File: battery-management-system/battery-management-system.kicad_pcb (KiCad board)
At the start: 4 copper layers, 130 x 100 mm, 216 parts, among them J1 CELL4_PLUS, J10 9V4, J11 5V, J12 18V, J13 3V3, J14 AMPHENOL_micro_usb_10118194-0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, J16 I2C, J17 UART_INTERCONNECT, J18 LEDS, J19 CHARGE/DISCHARGE, J2 CELL4_MINUS, J20 UART_USB, J21 rspro_header_5pin_3_5mm, J22 TEMP_CELL1, J23 TEMP_CELL2, J24 TEMP_CELL3, J25 TEMP_CELL4, J26 BALANCE_CONTROL, J27 BALANCE_INPUTS, J28 BALANCE_CURRENT, J3 CELL3_MINUS, J4 CELL2_MINUS, J5 CELL1_MINUS, J6 VBAT+, J7 VBAT+_CHARGE, J8 VBAT-, J9 -5V, Q1 DMN3730U, Q10 BS250FTA, Q11 BS250FTA, Q12 BS250FTA, Q13 BS250FTA, Q14 DMN3730U, Q15 DMN3404L, Q16 DMN3730U, Q17 DMN3730U, Q18 DMN3730U, Q19 DMN3730U, Q2 TJ40S04M3L, Q3 TJ40S04M3L, Q4 DMN3730U, Q5 DMN3730U, Q6 DMN3730U, Q7 DMN3730U, Q8 DMN3730U, Q9 DMN3730U, SW1 CELL4_PLUS, SW2 CELL4_MINUS, SW3 CELL3_PLUS, SW4 CELL3_MINUS, SW5 CELL2_PLUS, SW6 CELL2_MINUS, SW7 CELL1_PLUS, SW8 CELL1_MINUS, U1 ICL7660, U10 STC3100, U11 STM32L071CZTx, U12 LM2904M8-13, U13 LM2904M8-13, U14 LM2904M8-13, U15 LM2904M8-13, U16 MC74VHC139, U2 ICL7660, U3 L6982C33DR, U4 L6982C33DR, U5 ICL7660, U6 FT230XS, U7 ARM-JTAG-SWD, U8 AT24C512C, U9 NCT75DR2G

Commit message: update footprints and layout
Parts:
- removed C48: 90F, benediktibk:vishay_super_cap_form_g
- moved C46 10.2 mm to (67.1, 84.0)
- moved C47 0.50 mm to (67.1, 89.4), turned to 180 degrees
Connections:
- C46 pad 1: /BALANCE_CAP_MINUS_RAW -> /BALANCE_CAP_PLUS_RAW
- C46 pad 2: /BALANCE_CAP_PLUS_RAW -> /BALANCE_CAP_MINUS_RAW
- C47 pad 1: /BALANCE_CAP_MINUS_RAW -> /BALANCE_CAP_PLUS_RAW
- C47 pad 2: /BALANCE_CAP_PLUS_RAW -> /BALANCE_CAP_MINUS_RAW
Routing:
- net /BALANCE_CAP_MINUS_RAW: track 103.9 -> 86.5 mm, vias 0 -> 1
- net /BALANCE_CAP_PLUS_RAW: track 120.4 -> 105.5 mm

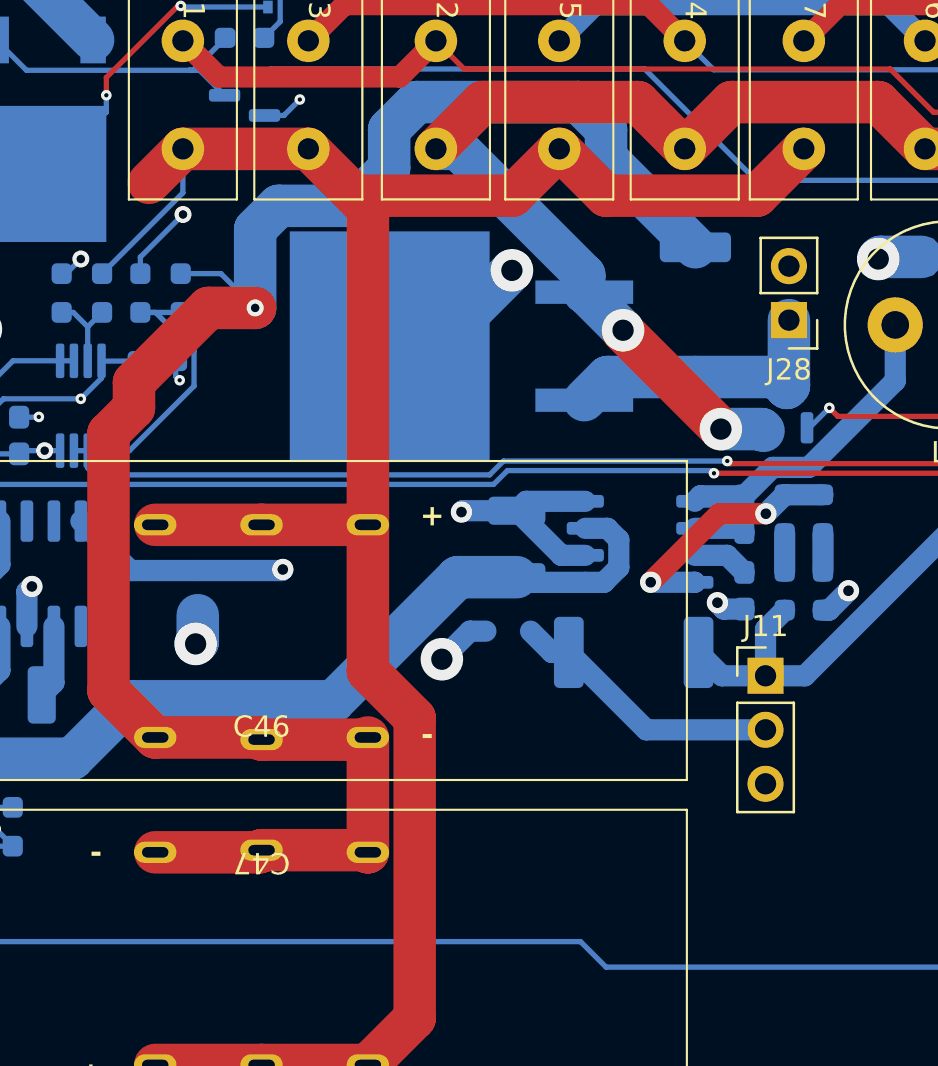
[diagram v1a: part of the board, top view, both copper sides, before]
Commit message: fix design rule errors
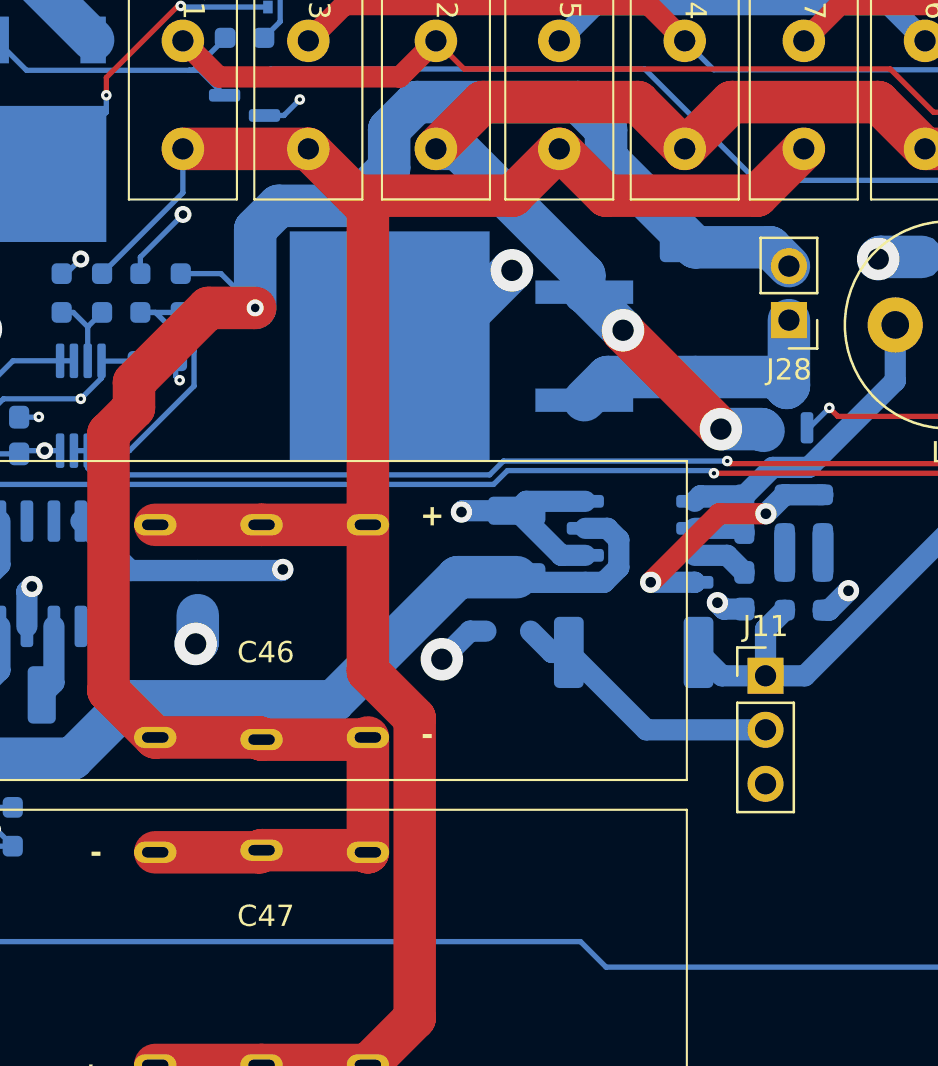
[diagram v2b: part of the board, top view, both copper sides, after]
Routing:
- net Net-(D10-K): track 111.9 -> 100.8 mm
- net /BALANCE_CAP_MINUS_RAW: track 86.5 -> 91.3 mm
- net /5V: track 262.1 -> 265.2 mm
- net /BALANCE_CAP_PLUS_RAW: track 105.5 -> 103.2 mm
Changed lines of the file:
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@@
     (property "ki_keywords" "cap capacitor")
     (attr through_hole)
-    (fp_text reference "C46" (at 0 -0.5 unlocked) (layer "F.SilkS")
+    (fp_text reference "C46" (at 0.2 -4 unlocked) (layer "F.SilkS")
         (effects (font (size 1 1) (thickness 0.15)))
     )
@@
     (property "ki_keywords" "cap capacitor")
     (attr through_hole)
-    (fp_text reference "C47" (at 0 -0.5 180 unlocked) (layer "F.SilkS")
+    (fp_text reference "C47" (at -0.2 -3 unlocked) (layer "F.SilkS")
         (effects (font (size 1 1) (thickness 0.15)))
     )
@@
   (via (at 39.3 93.3) (size 1) (drill 0.5) (layers "F.Cu" "B.Cu") (net 11))
   (via (at 86.3 115.8005) (size 2) (drill 1) (layers "F.Cu" "B.Cu") (net 11))
-  (segment (start 80.869848 92) (end 70.88873 92) (width 2) (layer "In1.Cu") (net 11))
-  (segment (start 39.83355 92.165001) (end 38.999275 92.999276) (width 2) (layer "In1.Cu") (net 11))
-  (segment (start 80.869848 92) (end 86.3 97.430152) (width 2) (layer "In1.Cu") (net 11))
-  (segment (start 45.6 93.160837) (end 44.604164 92.165001) (width 2) (layer "In1.Cu") (net 11))
-  (segment (start 47.008328 93.160837) (end 45.6 93.160837) (width 2) (layer "In1.Cu") (net 11))
-  (segment (start 70.88873 92) (end 62.044365 83.155635) (width 2) (layer "In1.Cu") (net 11))
-  (segment (start 44.604164 92.165001) (end 39.83355 92.165001) (width 2) (layer "In1.Cu") (net 11))
-  (segment (start 62.044365 81.855635) (end 56.662036 81.855635) (width 2) (layer "In1.Cu") (net 11))
-  (segment (start 86.3 97.430152) (end 86.3 115.8005) (width 2) (layer "In1.Cu") (net 11))
-  (segment (start 56.662036 81.855635) (end 56.662036 83.507129) (width 2) (layer "In1.Cu") (net 11))
-  (segment (start 62.044365 83.155635) (end 62.044365 81.855635) (width 2) (layer "In1.Cu") (net 11))
-  (segment (start 56.662036 83.507129) (end 47.008328 93.160837) (width 2) (layer "In1.Cu") (net 11))
+  (segment (start 86.3 115.8005) (end 86.3 97.430152) (width 2) (layer "In1.Cu") (net 11))
+  (segment (start 81.219848 92.35) (end 44.789163 92.35) (width 2) (layer "In1.Cu") (net 11))
+  (segment (start 44.604164 92.165001) (end 43.195836 92.165001) (width 2) (layer "In1.Cu") (net 11))
+  (segment (start 86.3 97.430152) (end 81.219848 92.35) (width 2) (layer "In1.Cu") (net 11))
+  (segment (start 39.648551 92.35) (end 38.999275 92.999276) (width 2) (layer "In1.Cu") (net 11))
+  (segment (start 43.010837 92.35) (end 39.648551 92.35) (width 2) (layer "In1.Cu") (net 11))
+  (segment (start 44.789163 92.35) (end 44.604164 92.165001) (width 2) (layer "In1.Cu") (net 11))
+  (segment (start 43.195836 92.165001) (end 43.010837 92.35) (width 2) (layer "In1.Cu") (net 11))
   (segment (start 88.0995 117.6) (end 86.3 115.8005) (width 1) (layer "B.Cu") (net 11))
   (segment (start 39.1 93.5) (end 39.3 93.3) (width 1) (layer "B.Cu") (net 11))
@@
   (segment (start 83.3 55.40873) (end 82.01127 54.12) (width 2) (layer "B.Cu") (net 12))
   (segment (start 73.1 55.40873) (end 73.1 57.23127) (width 2) (layer "B.Cu") (net 12))
+  (segment (start 91.015 60.95) (end 91.9 61.835) (width 2) (layer "B.Cu") (net 12))
+  (segment (start 87.5 60.95) (end 91.015 60.95) (width 2) (layer "B.Cu") (net 12))
   (segment (start 87.5 60.95) (end 83.3 56.75) (width 2) (layer "B.Cu") (net 12))
   (segment (start 67.9 59) (end 66.8 60.1) (width 2) (layer "B.Cu") (net 12))
@@
   (segment (start 67.1 99.4) (end 72.1 99.4) (width 2) (layer "F.Cu") (net 14))
   (segment (start 69.3 56.32) (end 71.5 58.52) (width 2) (layer "F.Cu") (net 14))
-  (segment (start 61.8 57.92) (end 63.4 56.32) (width 2) (layer "F.Cu") (net 14))
   (segment (start 72.1 80.88873) (end 74.3 83.08873) (width 2) (layer "F.Cu") (net 14))
   (segment (start 69.3 56.32) (end 63.4 56.32) (width 2) (layer "F.Cu") (net 14))
@@
   (via (at 125.9 38.8) (size 0.5) (drill 0.2) (layers "F.Cu" "B.Cu") (net 39))
   (via (at 68.1 76.1) (size 1) (drill 0.5) (layers "F.Cu" "B.Cu") (net 39))
+  (segment (start 61.516663 70.5125) (end 64.5 73.495837) (width 2) (layer "In1.Cu") (net 39))
   (segment (start 65.6 48.36) (end 65.6 61.8) (width 2) (layer "In1.Cu") (net 39))
-  (segment (start 75.578769 80.321231) (end 71.257538 76) (width 2) (layer "In1.Cu") (net 39))
   (segment (start 106.261 48.1) (end 117.05061 48.1) (width 2) (layer "In1.Cu") (net 39))
   (segment (start 118.99061 46.16) (end 121.95 49.11939) (width 2) (layer "In1.Cu") (net 39))
@@
   (segment (start 63.4 46.16) (end 65.6 48.36) (width 2) (layer "In1.Cu") (net 39))
   (segment (start 92.6 46.16) (end 87 46.16) (width 2) (layer "In1.Cu") (net 39))
+  (segment (start 66.295837 76.1) (end 71.357538 76.1) (width 2) (layer "In1.Cu") (net 39))
   (segment (start 121.95 49.11939) (end 121.95 59.6995) (width 2) (layer "In1.Cu") (net 39))
   (segment (start 65.6 61.8) (end 61 66.4) (width 2) (layer "In1.Cu") (net 39))
+  (segment (start 64.5 74.304163) (end 66.295837 76.1) (width 2) (layer "In1.Cu") (net 39))
   (segment (start 117.05061 48.1) (end 118.99061 46.16) (width 2) (layer "In1.Cu") (net 39))
   (segment (start 61 66.4) (end 61 69.01127) (width 2) (layer "In1.Cu") (net 39))
-  (segment (start 67.98873 76) (end 61 69.01127) (width 2) (layer "In1.Cu") (net 39))
+  (segment (start 66.295837 76.1) (end 68.1 76.1) (width 2) (layer "In1.Cu") (net 39))
   (segment (start 81.121231 80.321231) (end 75.578769 80.321231) (width 2) (layer "In1.Cu") (net 39))
   (segment (start 69.3 46.16) (end 75.3 46.16) (width 2) (layer "In1.Cu") (net 39))
   (segment (start 106.91 61.01) (end 106.625 60.725) (width 2) (layer "In1.Cu") (net 39))
+  (segment (start 64.5 73.495837) (end 64.5 74.304163) (width 2) (layer "In1.Cu") (net 39))
   (segment (start 98.3 46.16) (end 92.6 46.16) (width 2) (layer "In1.Cu") (net 39))
+  (segment (start 59.49877 70.5125) (end 61.516663 70.5125) (width 2) (layer "In1.Cu") (net 39))
   (segment (start 118.99061 46.16) (end 123.95 41.20061) (width 2) (layer "In1.Cu") (net 39))
   (segment (start 92.6 44.7) (end 90.9 43) (width 2) (layer "In1.Cu") (net 39))
-  (segment (start 71.257538 76) (end 67.98873 76) (width 2) (layer "In1.Cu") (net 39))
   (segment (start 59.49877 70.5125) (end 56.9 70.5125) (width 2) (layer "In1.Cu") (net 39))
   (segment (start 81.1 46.16) (end 75.3 46.16) (width 2) (layer "In1.Cu") (net 39))
@@
   (segment (start 81.1 46.16) (end 87 46.16) (width 2) (layer "In1.Cu") (net 39))
   (segment (start 125.14939 38.8) (end 125.9 38.8) (width 2) (layer "In1.Cu") (net 39))
+  (segment (start 71.357538 76.1) (end 75.578769 80.321231) (width 2) (layer "In1.Cu") (net 39))
   (segment (start 109.5 115) (end 109.5 108.7) (width 2) (layer "In1.Cu") (net 39))
   (segment (start 106.0005 48.3605) (end 106.261 48.1) (width 2) (layer "In1.Cu") (net 39))

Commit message: add enable input for cell measurement
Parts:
- removed the C2 at (55.2, 82.0)
- removed the C34 at (77.6, 42.7)
- removed C37, C39, C40, C42, C43: 100nF, benediktibk:C_0603_1608Metric_Pad1.08x0.95mm_HandSolder
- removed C41, C44: 1uF, benediktibk:C_0603_1608Metric_Pad1.08x0.95mm_HandSolder
- removed C46, C47: 90F, benediktibk:vishay_super_cap_form_g
- removed the C5 at (50.8, 78.3)
- removed D22, D23, D24, D25: BAS416, benediktibk:D_SOD-323
- removed the J10 at (126.9, 50.5)
- removed J26: BALANCE_CONTROL, benediktibk:PinHeader_1x05_P2.54mm_Vertical
- removed J27: BALANCE_INPUTS, benediktibk:PinHeader_1x05_P2.54mm_Vertical
- removed J28: BALANCE_CURRENT, benediktibk:PinHeader_1x02_P2.54mm_Vertical
- removed the J9 at (44.4, 82.9)
- removed the R47 at (59.6, 63.1)
- removed the R48 at (57.7, 63.1)
- removed the R49 at (63.3, 63.1)
- removed the R50 at (61.4, 63.1)
- removed R59: 100kOhm, benediktibk:R_0603_1608Metric_Pad0.98x0.95mm_HandSolder
- removed the R6 at (47.0, 76.9)
- removed R60, R61: 10kOhm, benediktibk:R_0603_1608Metric_Pad0.98x0.95mm_HandSolder
- removed R62: 220kOhm, benediktibk:R_0603_1608Metric_Pad0.98x0.95mm_HandSolder
- removed R63: 4Ohm, benediktibk:TO-263-resistor
- removed R64: 2mOhm, benediktibk:R_2512_6332Metric_Pad1.40x3.35mm_HandSolder
- removed the R7 at (123.0, 53.2)
- removed SW1: CELL4_PLUS, benediktibk:SIL05-1A72-BV669
- removed SW2: CELL4_MINUS, benediktibk:SIL05-1A72-BV669
- removed SW3: CELL3_PLUS, benediktibk:SIL05-1A72-BV669
- removed SW4: CELL3_MINUS, benediktibk:SIL05-1A72-BV669
- removed SW5: CELL2_PLUS, benediktibk:SIL05-1A72-BV669
- removed SW6: CELL2_MINUS, benediktibk:SIL05-1A72-BV669
- removed SW7: CELL1_PLUS, benediktibk:SIL05-1A72-BV669
- removed SW8: CELL1_MINUS, benediktibk:SIL05-1A72-BV669
- removed the U13 at (58.6, 68.4)
- removed U15: LM2904M8-13, benediktibk:MSOP-8_3x3mm_P0.65mm
- removed the U2 at (56.7, 76.3)
- added H4: MountingHole_Pad, benediktibk:MountingHole_6.4mm_M6_Pad_TopBottom, F.Cu at (28.0, 152.0)
- added J23: Conn_01x05, benediktibk:PinHeader_1x05_P2.54mm_Vertical, F.Cu at (48.8, 131.8)
- added L10: L_220µH_1A, benediktibk:L_Wuerth_HCI-1050, B.Cu at (66.0, 83.0)
- added L3: L_220µH_1A, benediktibk:L_Wuerth_HCI-1050, B.Cu at (92.0, 44.0)
- added L4: L_220µH_1A, benediktibk:L_Wuerth_HCI-1050, B.Cu at (92.0, 57.0)
- added L5: L_220µH_1A, benediktibk:L_Wuerth_HCI-1050, B.Cu at (92.0, 70.0)
- added L6: L_220µH_1A, benediktibk:L_Wuerth_HCI-1050, B.Cu at (92.0, 83.0)
- added L7: L_220µH_1A, benediktibk:L_Wuerth_HCI-1050, B.Cu at (79.0, 83.0)
- added L8: L_220µH_1A, benediktibk:L_Wuerth_HCI-1050, B.Cu at (79.0, 70.0)
- added L9: L_220µH_1A, benediktibk:L_Wuerth_HCI-1050, B.Cu at (66.0, 70.0)
- added Q20: DMN3404L, benediktibk:SOT-23, B.Cu at (40.0, 66.0)
- added Q21: DMN3404L, benediktibk:SOT-23, B.Cu at (101.0, 73.0)
- added Q22: DMN3404L, benediktibk:SOT-23, B.Cu at (101.0, 43.0)
- added Q23: DMN3404L, benediktibk:SOT-23, B.Cu at (40.0, 50.0)
- added Q24: DMN3404L, benediktibk:SOT-23, B.Cu at (45.0, 55.0)
- added Q25: DMN3404L, benediktibk:SOT-23, B.Cu at (101.0, 58.0)
- added Q26: DMN3404L, benediktibk:SOT-23, B.Cu at (101.0, 68.0)
- added Q27: DMN3404L, benediktibk:SOT-23, B.Cu at (45.0, 61.0)
- added Q28: DMN3404L, benediktibk:SOT-23, B.Cu at (45.0, 66.0)
- added Q29: DMN3404L, benediktibk:SOT-23, B.Cu at (101.0, 78.0)
- added Q30: DMN3404L, benediktibk:SOT-23, B.Cu at (101.0, 83.0)
- added Q31: DMN3404L, benediktibk:SOT-23, B.Cu at (101.0, 48.0)
- added Q32: DMN3404L, benediktibk:SOT-23, B.Cu at (101.0, 87.8)
- added Q33: DMN3404L, benediktibk:SOT-23, B.Cu at (51.0, 66.1)
- added Q34: DMN3404L, benediktibk:SOT-23, B.Cu at (49.9, 56.0)
- added Q35: DMN3404L, benediktibk:SOT-23, B.Cu at (83.4, 43.8)
- added Q36: DMN3404L, benediktibk:SOT-23, B.Cu at (96.7, 91.1)
- added Q37: DMN3404L, benediktibk:SOT-23, B.Cu at (111.3, 94.2)
- added Q38: TJ40S04M3L, benediktibk:TO-252-2, B.Cu at (103.9, 95.9)
- added R52: 10kOhm, benediktibk:R_0603_1608Metric_Pad0.98x0.95mm_HandSolder, B.Cu at (104.0, 87.8)
- added R53: 10kOhm, benediktibk:R_0603_1608Metric_Pad0.98x0.95mm_HandSolder, B.Cu at (51.1, 63.2)
- added R54: 10kOhm, benediktibk:R_0603_1608Metric_Pad0.98x0.95mm_HandSolder, B.Cu at (49.8, 58.8)
- added R55: 10kOhm, benediktibk:R_0603_1608Metric_Pad0.98x0.95mm_HandSolder, B.Cu at (83.2, 46.8)
- added R56: 10kOhm, benediktibk:R_0603_1608Metric_Pad0.98x0.95mm_HandSolder, B.Cu at (93.7, 91.1)
- added R57: 220kOhm, benediktibk:R_0603_1608Metric_Pad0.98x0.95mm_HandSolder, B.Cu at (108.6, 93.4)
- Q1, Q14, Q16, Q17, Q18, Q19, Q4, Q5, Q6, Q7, Q8, Q9: value DMN3730U -> DMN3404L
- moved C22 138.4 mm to (259.3, 124.9)
- moved C23 138.4 mm to (210.8, 142.3)
- moved C24 138.4 mm to (248.3, 141.4)
- moved C27 138.4 mm to (259.6, 129.8)
- moved C28 138.4 mm to (259.6, 134.9)
- moved C32 138.4 mm to (209.8, 85.3)
- moved D19 138.4 mm to (276.3, 88.5)
- moved D20 138.4 mm to (276.3, 85.8)
- moved D21 138.4 mm to (276.3, 83.3)
- moved J12 138.4 mm to (153.8, 140.9)
- moved J13 138.4 mm to (228.2, 148.9)
- moved J15 138.4 mm to (279.8, 88.4)
- moved Q6 138.4 mm to (276.3, 89.2)
- moved Q7 138.4 mm to (276.3, 85.0)
- moved Q8 138.4 mm to (276.3, 80.8)
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- renumbered C12 to C10, C13 to C11, C14 to C12, C15 to C13, C16 to C14, C17 to C15, C18 to C16, C19 to C17, C20 to C18, C21 to C19, C3 to C2, C22 to C20, C23 to C21, C24 to C22, C25 to C23, C26 to C24, C27 to C25, C28 to C26, C29 to C27, C30 to C28, C31 to C29, C4 to C3, C32 to C30, C33 to C31, C35 to C32, C36 to C33, C38 to C34, C45 to C35, C6 to C4, C7 to C5, C8 to C6, C9 to C7, C10 to C8, C11 to C9, J12 to J10, J13 to J11, J14 to J12, J16 to J13, J17 to J14, J18 to J15, J19 to J16, J20 to J17, J21 to J18, J22 to J19, J23 to J20, J24 to J21, J25 to J22, J11 to J9, R12 to R10, R13 to R11, R14 to R12, R15 to R13, R16 to R14, R17 to R15, R18 to R16, R19 to R17, R20 to R18, R21 to R19, R22 to R20, R23 to R21, R24 to R22, R25 to R23, R26 to R24, R27 to R25, R29 to R26, R30 to R27, R31 to R28, R32 to R29, R33 to R30, R34 to R31, R35 to R32, R36 to R33, R37 to R34, R38 to R35, R39 to R36, R40 to R37, R41 to R38, R42 to R39, R43 to R40, R44 to R41, R45 to R42, R46 to R43, R51 to R44, R52 to R45, R53 to R46, R54 to R47, R55 to R48, R56 to R49, R57 to R50, R58 to R51, R8 to R6, R9 to R7, R10 to R8, R11 to R9, U11 to U10, U12 to U11, U14 to U12, U16 to U13, U3 to U2, U4 to U3, U5 to U4, U6 to U5, U7 to U6, U8 to U7, U9 to U8, U10 to U9
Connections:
- C32 pad 2: /-5V -> GND
- C34 pad 2: /-5V -> GND
- D12 pad 2: Net-(D12-A) -> /Power Supply/9V4
- Q14 pad 1: /LIMIT_BALANCING_CURRENT -> /Cell Balancing/CHARGE_CELL4
- Q14 pad 2: GND -> /Battery Pack/PACK
- Q15 pad 1: Net-(Q14-D) -> /Cell Balancing/CHARGE_CELL4
- Q15 pad 3: Net-(J28-Pin_1) -> /Battery Pack/CELL4_MINUS
- Q16 pad 1: Net-(Q16-G) -> /Cell Balancing/CHARGE_CELL3
- Q16 pad 2: GND -> /Battery Pack/CELL4_MINUS
- Q16 pad 3: /Cell Balancing/CELL1 -> Net-(Q16-D)
- Q17 pad 1: Net-(Q17-G) -> /Cell Balancing/CHARGE_CELL3
- Q17 pad 2: GND -> Net-(Q17-S)
- Q17 pad 3: /Cell Balancing/CELL2 -> /Battery Pack/CELL3_MINUS
- Q18 pad 1: Net-(Q18-G) -> /Cell Balancing/CHARGE_CELL2
- Q18 pad 2: GND -> /Battery Pack/CELL3_MINUS
- Q18 pad 3: /Cell Balancing/CELL3 -> Net-(Q18-D)
- Q19 pad 1: Net-(Q19-G) -> /Cell Balancing/CHARGE_CELL2
- Q19 pad 2: GND -> Net-(Q19-S)
- Q19 pad 3: /Cell Balancing/CELL4 -> /Battery Pack/CELL2_MINUS
- U10 pad 14: /Cell Measurement/BALANCE_CAP_PLUS -> unconnected-(U10-PA4-Pad14)
- U10 pad 15: /Cell Measurement/BALANCE_CAP_MINUS -> unconnected-(U10-PA5-Pad15)
- U10 pad 38: /DISCHARGE -> /CELL_BALANCING_STROBE
- U10 pad 41: /LIMIT_BALANCING_CURRENT -> /DISCHARGE
- U11 pad 4: /-5V -> GND
- U12 pad 4: /-5V -> GND
- U13 pad 1: /EN_CELL_BALANCING -> /CELL_BALANCING_STROBE
- U13 pad 4: Net-(Q16-G) -> Net-(Q32-G)
- U13 pad 5: Net-(Q17-G) -> Net-(Q33-G)
- U13 pad 6: Net-(Q18-G) -> Net-(Q34-G)
- U13 pad 7: Net-(Q19-G) -> Net-(Q35-G)
- U4 pad 8: Net-(D12-A) -> /Power Supply/9V4
- U9 pad 6: /Cell Measurement/CURRENT_SENSE -> /Battery Pack/CELL1_MINUS
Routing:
- net /5V: track 265.2 -> 0.00 mm, vias 7 -> 0
- net GND: track 244.0 -> 32.8 mm, vias 55 -> 15
- net Net-(Q22-S): track 0.00 -> 166.6 mm, vias 0 -> 3
- net /MCU/SCL: track 162.9 -> 0.00 mm, vias 1 -> 0
- net /MCU/SDA: track 161.5 -> 0.00 mm, vias 1 -> 0
- net /-5V: track 158.2 -> 0.00 mm, vias 6 -> 0
- net Net-(Q23-S): track 0.00 -> 123.1 mm
- net /Cell Measurement/CELL3: track 117.0 -> 0.00 mm, vias 2 -> 0
- net /Cell Measurement/CELL4: track 115.6 -> 0.00 mm, vias 2 -> 0
- net /18V: track 26.3 -> 139.2 mm, vias 2 -> 5
- net /Cell Balancing/CHARGE_CELL2: track 0.00 -> 103.6 mm, vias 0 -> 4
- net /BALANCE_CAP_PLUS_RAW: track 103.2 -> 0.00 mm
- net Net-(D10-K): track 100.8 -> 0.00 mm, vias 2 -> 0
- net /Cell Balancing/CHARGE_CELL3: track 0.00 -> 99.3 mm, vias 0 -> 3
- net /Cell Measurement/CELL2: track 99.0 -> 0.00 mm, vias 2 -> 0
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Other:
- board size 130 x 100 mm -> 100 x 140 mm

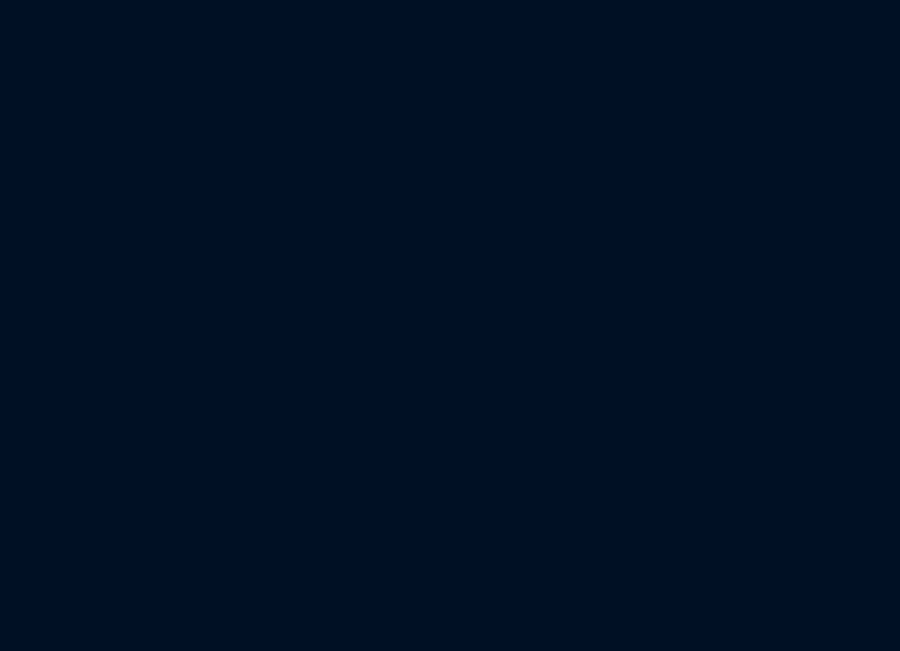
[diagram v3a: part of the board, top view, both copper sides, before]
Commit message: make layout easier for cell measurement
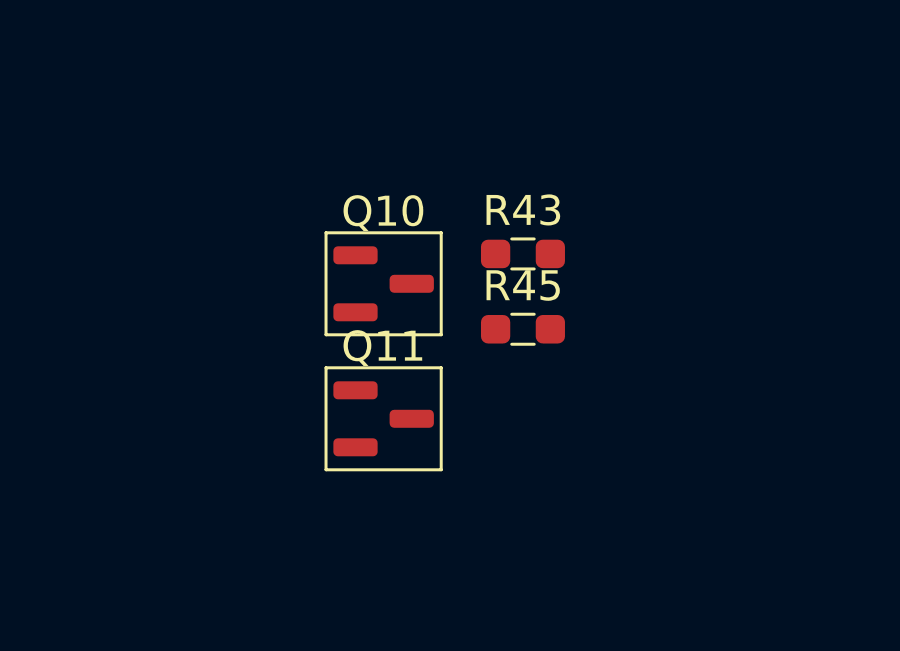
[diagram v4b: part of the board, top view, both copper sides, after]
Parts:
- added Q10: DMN3404L, benediktibk:SOT-23, F.Cu at (170.4, 34.8)
- added Q11: BS250FTA, benediktibk:SOT-23, F.Cu at (170.4, 39.2)
- added R43: 220kOhm, benediktibk:R_0603_1608Metric_Pad0.98x0.95mm_HandSolder, F.Cu at (175.0, 33.8)
- added R45: 220kOhm, benediktibk:R_0603_1608Metric_Pad0.98x0.95mm_HandSolder, F.Cu at (175.0, 36.3)
- renumbered Q10 to Q12, Q11 to Q13, Q12 to Q14, Q13 to Q15, Q14 to Q16, Q15 to Q17, Q16 to Q18, Q17 to Q19, Q18 to Q20, Q19 to Q21, Q20 to Q22, Q21 to Q23, Q22 to Q24, Q23 to Q25, Q24 to Q26, Q25 to Q27, Q26 to Q28, Q27 to Q29, Q28 to Q30, Q29 to Q31, Q30 to Q32, Q31 to Q33, Q32 to Q34, Q33 to Q35, Q34 to Q36, Q35 to Q37, Q36 to Q38, Q37 to Q39, Q38 to Q40, R43 to R44, R44 to R46, R45 to R47, R46 to R48, R47 to R49, R48 to R50, R49 to R51, R50 to R52, R51 to R53, R52 to R54, R53 to R55, R54 to R56, R55 to R57, R56 to R58, R57 to R59
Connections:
- C31 pad 1: /5V -> Net-(Q11-D)
- C32 pad 1: /5V -> Net-(Q11-D)
- C33 pad 1: /5V -> Net-(Q11-D)
- C34 pad 1: /5V -> Net-(Q11-D)
- Q9 pad 1: /18V -> /EN_CELL_MEASUREMENT
- R42 pad 1: /18V -> /EN_CELL_MEASUREMENT
- R48 pad 2: Net-(U11A-+) -> Net-(U12B-+)
- R49 pad 1: Net-(U11A-+) -> Net-(U12B-+)
- R50 pad 2: Net-(U12B-+) -> Net-(U11A-+)
- R51 pad 1: Net-(U12B-+) -> Net-(U11A-+)
- U10 pad 20: unconnected-(U10-PB2-Pad20) -> /EN_CELL_MEASUREMENT
- U11 pad 1: /Cell Measurement/CELL3 -> /Cell Measurement/CELL2
- U11 pad 2: /Cell Measurement/CELL3 -> /Cell Measurement/CELL2
- U11 pad 8: /5V -> Net-(Q11-D)
- U12 pad 6: /Cell Measurement/CELL2 -> /Cell Measurement/CELL3
- U12 pad 7: /Cell Measurement/CELL2 -> /Cell Measurement/CELL3
- U12 pad 8: /5V -> Net-(Q11-D)
